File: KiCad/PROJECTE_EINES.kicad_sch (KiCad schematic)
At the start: 0 parts

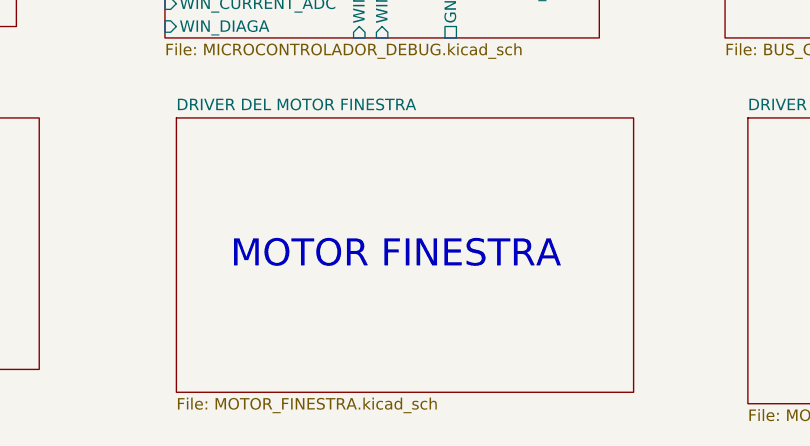
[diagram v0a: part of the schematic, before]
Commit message: Actulització etapa d'alimentació
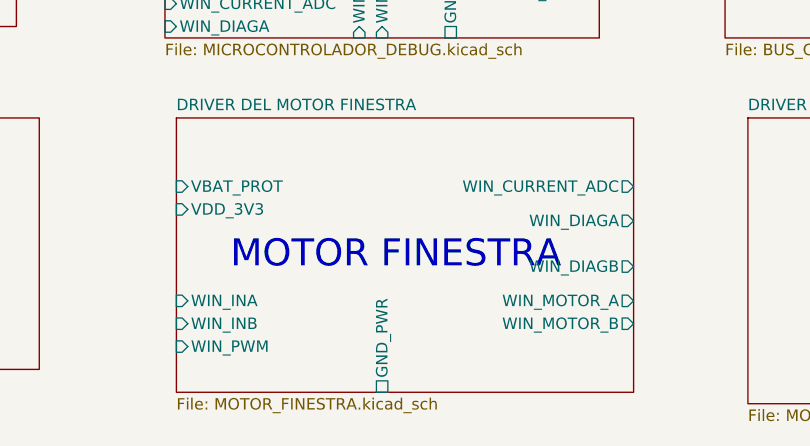
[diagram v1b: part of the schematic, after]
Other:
- sheet DRIVER DEL MOTOR FINESTRA ports: added GND_PWR, VBAT_PROT, VDD_3V3, WIN_CURRENT_ADC, WIN_DIAGA, WIN_DIAGB, WIN_INA, WIN_INB, WIN_MOTOR_A, WIN_MOTOR_B, WIN_PWM; removed none
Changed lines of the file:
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@@
+			)
+		)
+		(pin "GND_PWR" passive
+			(at 106.68 91.44 270)
+			(effects
+				(font
+					(size 1.27 1.27)
+				)
+				(justify left)
+			)
+		)
+		(pin "VBAT_PROT" input
+			(at 83.82 68.58 180)
+			(effects
+				(font
+					(size 1.27 1.27)
+				)
+				(justify left)
+			)
+		)
+		(pin "VDD_3V3" input
+			(at 83.82 71.12 180)
+			(effects
+				(font
+					(size 1.27 1.27)
+				)
+				(justify left)
+			)
+		)
+		(pin "WIN_CURRENT_ADC" output
+			(at 134.62 68.58 0)
+			(effects
+				(font
+					(size 1.27 1.27)
+				)
+				(justify right)
+			)
+		)
+		(pin "WIN_DIAGA" output
+			(at 134.62 72.39 0)
+			(effects
+				(font
+					(size 1.27 1.27)
+				)
+				(justify right)
+			)
+		)
+		(pin "WIN_DIAGB" output
+			(at 134.62 77.47 0)
+			(effects
+				(font
+					(size 1.27 1.27)
+				)
+				(justify right)
+			)
+		)
+		(pin "WIN_INA" input
+			(at 83.82 81.28 180)
+			(effects
+				(font
+					(size 1.27 1.27)
+				)
+				(justify left)
+			)
+		)
+		(pin "WIN_INB" input
+			(at 83.82 83.82 180)
+			(effects
+				(font
+					(size 1.27 1.27)
+				)
+				(justify left)
+			)
+		)
+		(pin "WIN_MOTOR_A" output
+			(at 134.62 81.28 0)
+			(effects
+				(font
+					(size 1.27 1.27)
+				)
+				(justify right)
+			)
+		)
+		(pin "WIN_MOTOR_B" output
+			(at 134.62 83.82 0)
+			(effects
+				(font
+					(size 1.27 1.27)
+				)
+				(justify right)
+			)
+		)
+		(pin "WIN_PWM" input
+			(at 83.82 86.36 180)
+			(effects
+				(font
+					(size 1.27 1.27)
+				)
+				(justify left)
 			)
 		)

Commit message: Actualització README
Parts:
- added R2: 0, symbol Device:R
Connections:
- new net GND: R2.2
- new net GNDPWR: R2.1
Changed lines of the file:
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@@
+		)
+	)
+	(wire
+		(pts
+			(xy 57.15 128.27) (xy 66.04 128.27)
+		)
+		(stroke
+			(width 0)
+			(type default)
+		)
+	)
+	(wire
+		(pts
+			(xy 41.91 128.27) (xy 49.53 128.27)
+		)
+		(stroke
+			(width 0)
+			(type default)
+		)
+	)
+	(symbol
+		(lib_id "power:GNDPWR")
+		(at 41.91 128.27 0)
+		(unit 1)
+		(exclude_from_sim no)
+		(in_bom yes)
+		(on_board yes)
+		(dnp no)
+		(fields_autoplaced yes)
+		(property "Reference" "#PWR05"
+			(at 41.91 133.35 0)
+			(effects
+				(font
+					(size 1.27 1.27)
+				)
+				(hide yes)
+			)
+		)
+		(property "Value" "GNDPWR"
+			(at 41.783 132.08 0)
+			(effects
+				(font
+					(size 1.27 1.27)
+				)
+			)
+		)
+		(property "Footprint" ""
+			(at 41.91 129.54 0)
+			(effects
+				(font
+					(size 1.27 1.27)
+				)
+				(hide yes)
+			)
+		)
+		(property "Datasheet" ""
+			(at 41.91 129.54 0)
+			(effects
+				(font
+					(size 1.27 1.27)
+				)
+				(hide yes)
+			)
+		)
+		(property "Description" "Power symbol creates a global label with name \"GNDPWR\" , global ground"
+			(at 41.91 128.27 0)
+			(effects
+				(font
+					(size 1.27 1.27)
+				)
+				(hide yes)
+			)
+		)
+		(pin "1"
+		)
+		(instances
+			(project ""
+				(path "/347831db-5db9-4aff-ad32-e56fd770e219"
+					(reference "#PWR05")
+					(unit 1)
+				)
+			)
+		)
+	)
+	(symbol
+		(lib_id "power:GND")
+		(at 66.04 128.27 0)
+		(unit 1)
+		(exclude_from_sim no)
+		(in_bom yes)
+		(on_board yes)
+		(dnp no)
+		(fields_autoplaced yes)
+		(property "Reference" "#PWR06"
+			(at 66.04 134.62 0)
+			(effects
+				(font
+					(size 1.27 1.27)
+				)
+				(hide yes)
+			)
+		)
+		(property "Value" "GND"
+			(at 66.04 133.35 0)
+			(effects
+				(font
+					(size 1.27 1.27)
+				)
+			)
+		)
+		(property "Footprint" ""
+			(at 66.04 128.27 0)
+			(effects
+				(font
+					(size 1.27 1.27)
+				)
+				(hide yes)
+			)
+		)
+		(property "Datasheet" ""
+			(at 66.04 128.27 0)
+			(effects
+				(font
+					(size 1.27 1.27)
+				)
+				(hide yes)
+			)
+		)
+		(property "Description" "Power symbol creates a global label with name \"GND\" , ground"
+			(at 66.04 128.27 0)
+			(effects
+				(font
+					(size 1.27 1.27)
+				)
+				(hide yes)
+			)
+		)
+		(pin "1"
+		)
+		(instances
+			(project ""
+				(path "/347831db-5db9-4aff-ad32-e56fd770e219"
+					(reference "#PWR06")
+					(unit 1)
+				)
+			)
+		)
+	)
+	(symbol
+		(lib_id "Device:R")
+		(at 53.34 128.27 90)
+		(unit 1)
+		(exclude_from_sim no)
+		(in_bom yes)
+		(on_board yes)
+		(dnp no)
+		(fields_autoplaced yes)
+		(property "Reference" "R2"
+			(at 53.34 121.92 90)
+			(effects
+				(font
+					(size 1.27 1.27)
+				)
+			)
+		)
+		(property "Value" "0"
+			(at 53.34 124.46 90)
+			(effects
+				(font
+					(size 1.27 1.27)
+				)
+			)
+		)
+		(property "Footprint" ""
+			(at 53.34 130.048 90)
+			(effects
+				(font
+					(size 1.27 1.27)
+				)
+				(hide yes)
+			)
+		)
+		(property "Datasheet" "~"
+			(at 53.34 128.27 0)
+			(effects
+				(font
+					(size 1.27 1.27)
+				)
+				(hide yes)
+			)
+		)
+		(property "Description" "Resistor"
+			(at 53.34 128.27 0)
+			(effects
+				(font
+					(size 1.27 1.27)
+				)
+				(hide yes)
+			)
+		)
+		(pin "2"
+		)
+		(pin "1"
+		)
+		(instances
+			(project "PROJECTE_EINES"
+				(path "/347831db-5db9-4aff-ad32-e56fd770e219"
+					(reference "R2")
+					(unit 1)
+				)
+			)
 		)
 	)

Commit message: Actualització Sheet Inputs
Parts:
- added J3: J_DEBUG, symbol Connector:Conn_01x05_Pin
- added J_PWR1: Conn_01x02_Pin, symbol Connector:Conn_01x02_Pin
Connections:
- net GND: now also J3.3 (Pin_3)
- net GNDPWR: now also J_PWR1.2 (Pin_2)
- new net MCLR: J3.1 (Pin_1)
- new net PGEC1: J3.5 (Pin_5)
- new net PGED1: J3.4 (Pin_4)
- new net VBAT_12V: J_PWR1.1 (Pin_1)
- new net VDD_3V3: J3.2 (Pin_2)
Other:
- sheet INPUTS ports: added GND, MCLR, PGEC1, PGED1, VDD_3V3, WIN_BTN_DOWN, WIN_BTN_UP, WIN_LIMIT; removed none
- moved on the sheet: R2

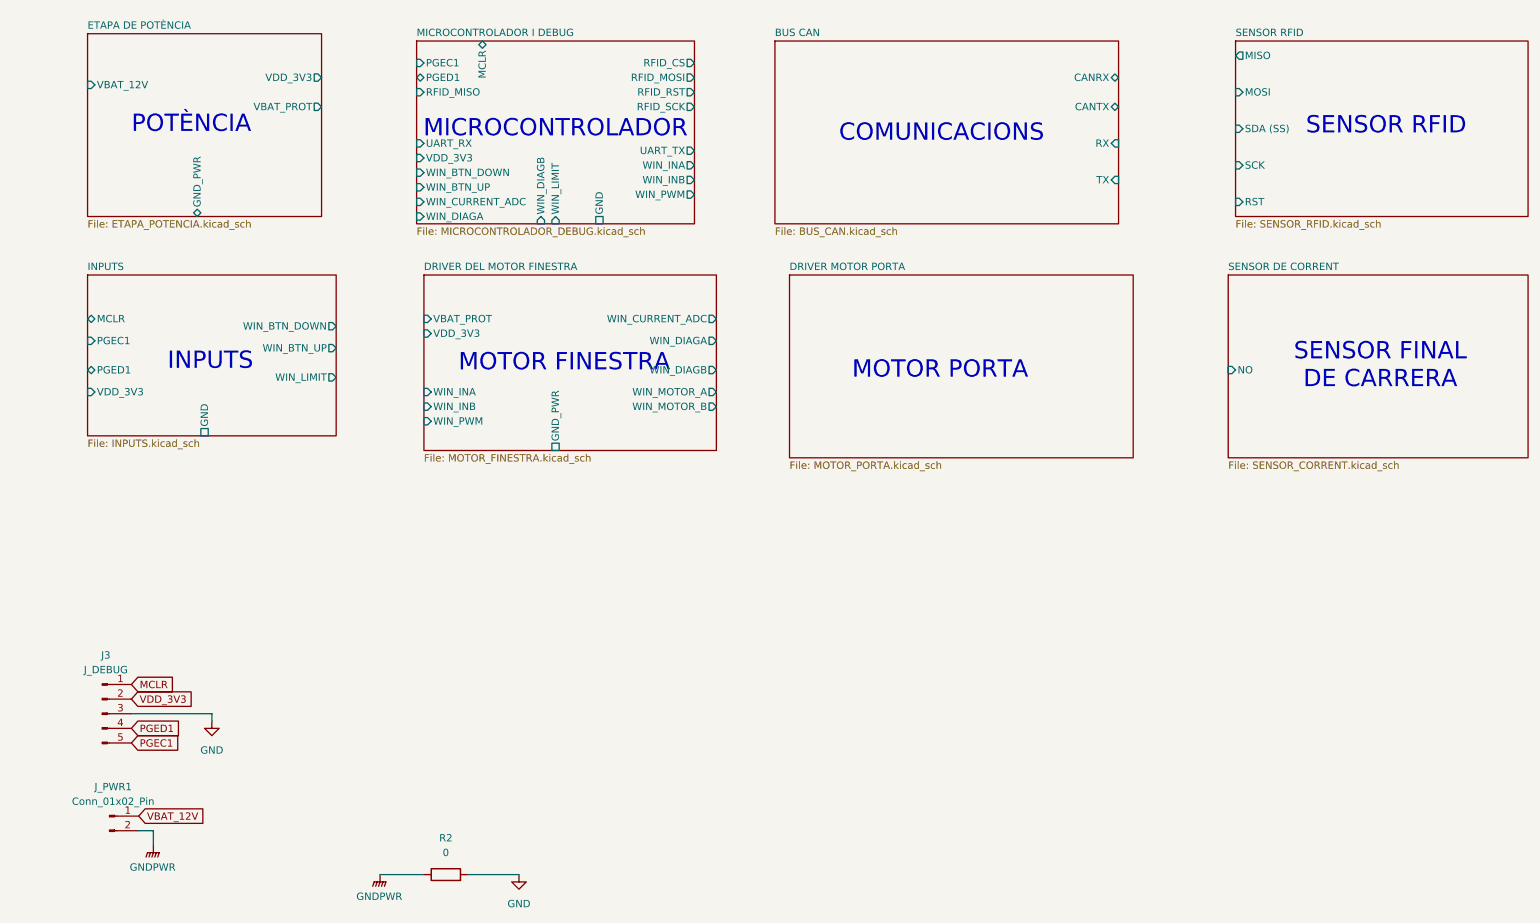
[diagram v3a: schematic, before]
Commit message: Esquematic general conectat
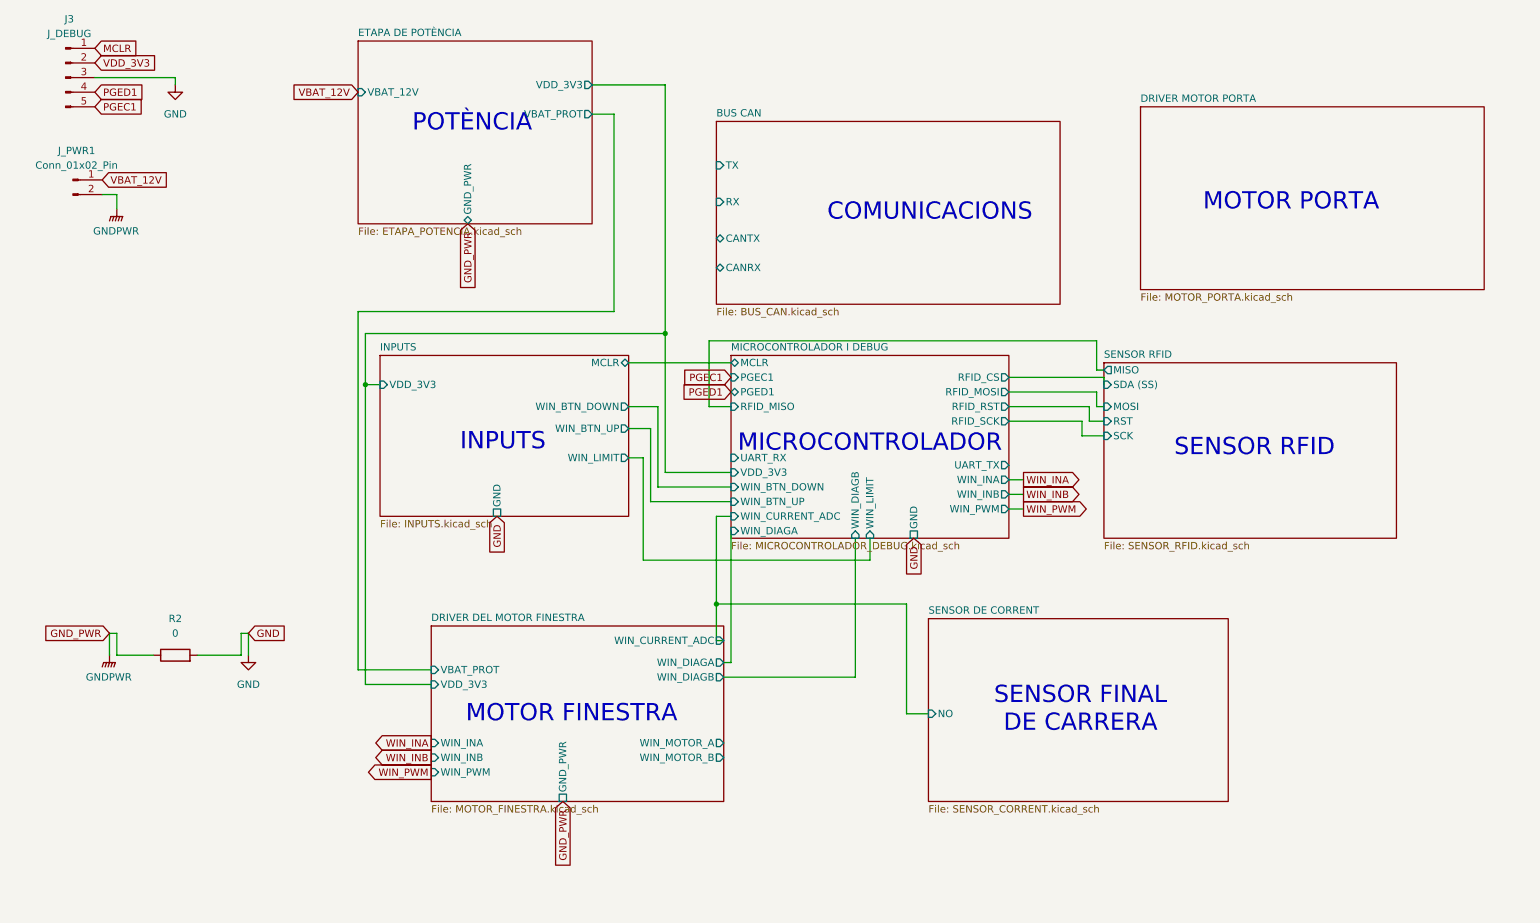
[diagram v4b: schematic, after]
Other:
- sheet INPUTS ports: added none; removed PGEC1, PGED1
- moved on the sheet: J3, J_PWR1, R2

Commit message: ESQUEMATIC FINAL V.1
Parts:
- added J_MOTOR_WIN: Conn_01x02_Pin, symbol Connector:Conn_01x02_Pin
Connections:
- new net WIN_MOTOR_A: J_MOTOR_WIN.1 (Pin_1)
- new net WIN_MOTOR_B: J_MOTOR_WIN.2 (Pin_2)
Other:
- moved on the sheet: R2

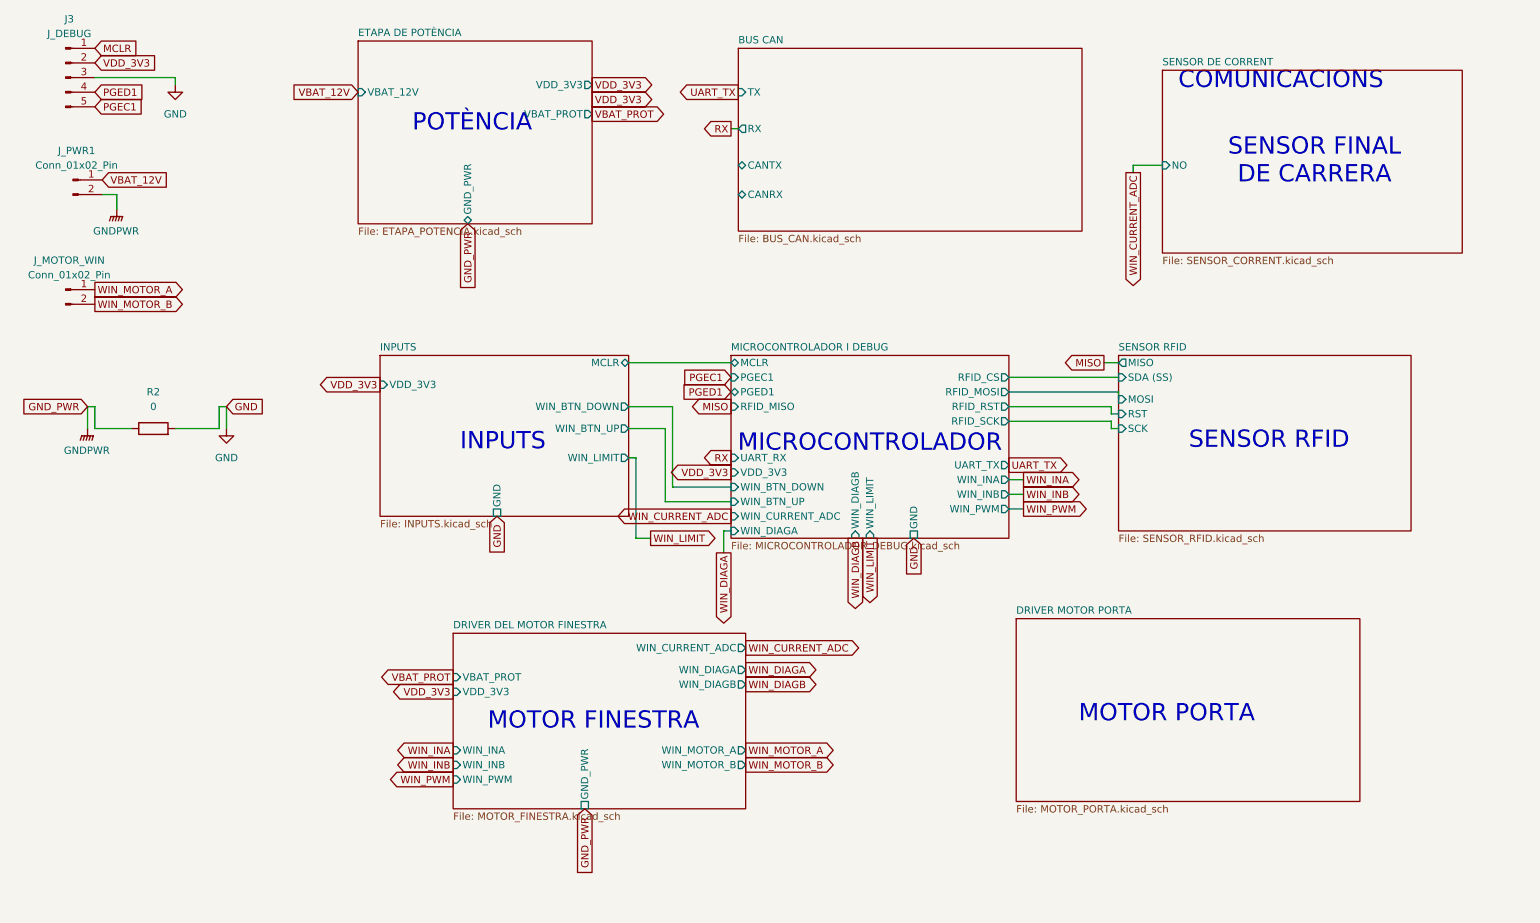
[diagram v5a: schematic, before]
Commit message: Nova versió diagrama de blocs + BOM actualitzat + Nova versió KiCad
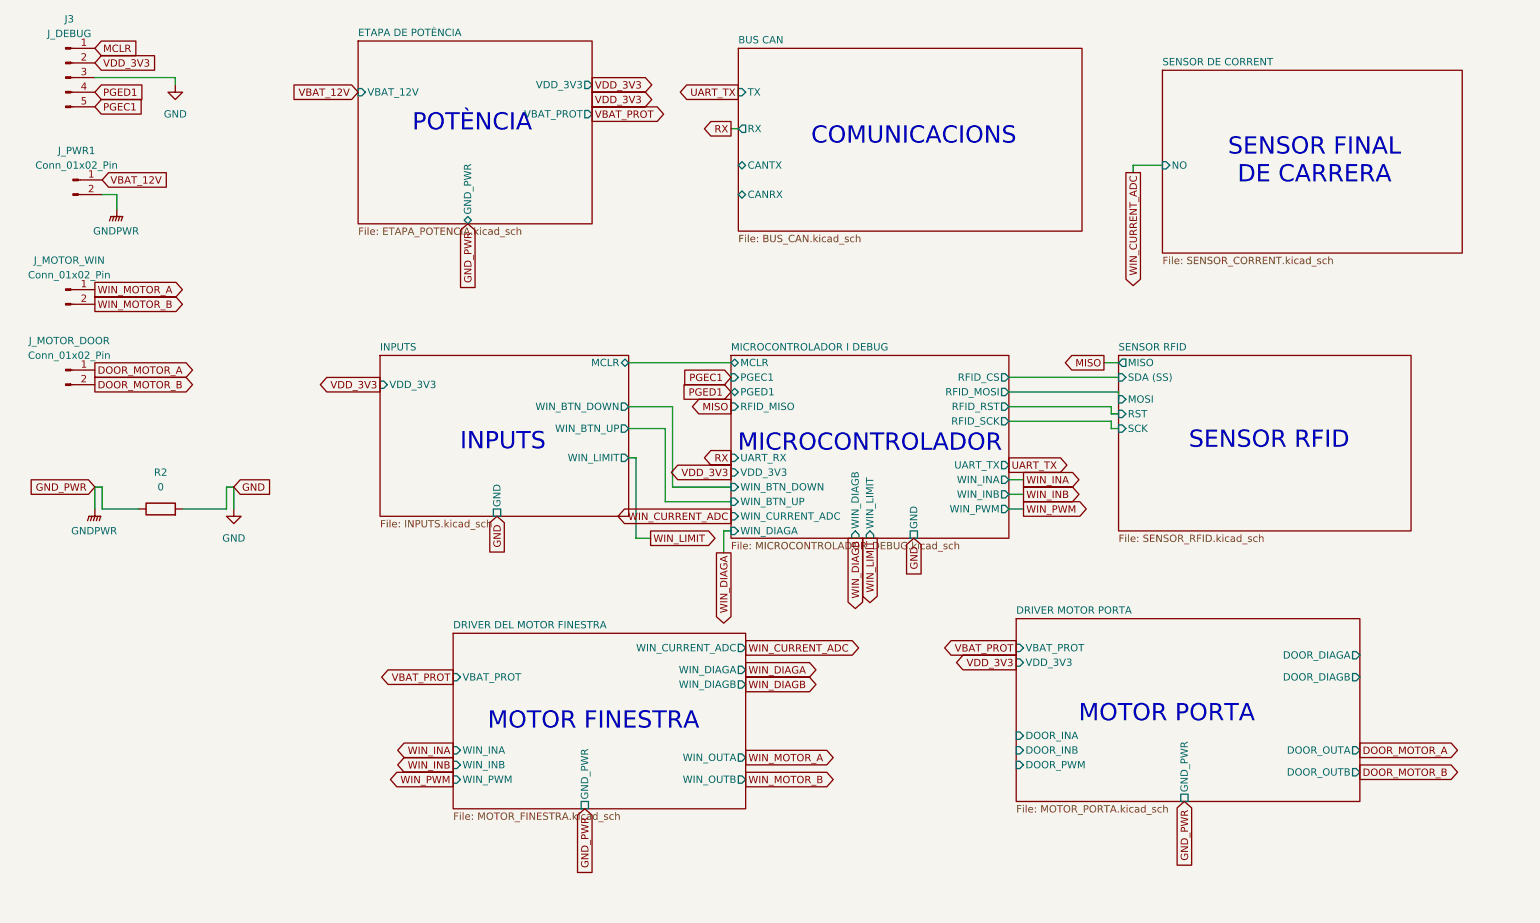
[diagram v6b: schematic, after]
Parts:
- added J_MOTOR_DOOR: Conn_01x02_Pin, symbol Connector:Conn_01x02_Pin
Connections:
- new net DOOR_MOTOR_A: J_MOTOR_DOOR.1 (Pin_1)
- new net DOOR_MOTOR_B: J_MOTOR_DOOR.2 (Pin_2)
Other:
- sheet DRIVER DEL MOTOR FINESTRA ports: added WIN_OUTA, WIN_OUTB; removed VDD_3V3, WIN_MOTOR_A, WIN_MOTOR_B
- sheet DRIVER MOTOR PORTA ports: added DOOR_DIAGA, DOOR_DIAGB, DOOR_INA, DOOR_INB, DOOR_OUTA, DOOR_OUTB, DOOR_PWM, GND_PWR, VBAT_PROT, VDD_3V3; removed none
- moved on the sheet: R2

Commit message: Resistències pull-up arreglades als motors
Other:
- sheet DRIVER DEL MOTOR FINESTRA ports: added VDD_3V3; removed none
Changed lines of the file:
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@@
+		)
+	)
+	(global_label "VDD_3V3"
+		(shape output)
+		(at 88.9 127 180)
+		(effects
+			(font
+				(size 1.27 1.27)
+			)
+			(justify right)
+		)
+		(property "Intersheetrefs" "${INTERSHEET_REFS}"
+			(at 88.9 127 0)
+			(effects
+				(font
+					(size 1.27 1.27)
+				)
+				(hide yes)
+			)
 		)
 	)
@@
 			)
 		)
+		(pin "VDD_3V3" input
+			(at 88.9 127 180)
+			(effects
+				(font
+					(size 1.27 1.27)
+				)
+				(justify left)
+			)
+		)
